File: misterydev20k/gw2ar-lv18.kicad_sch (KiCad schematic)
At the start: 53 parts, among them J3 JTAG, U5 GW2AR-LV18-QN88, U6 W25Q128JVS, U8 SY8113BADC, Y2 27MHz

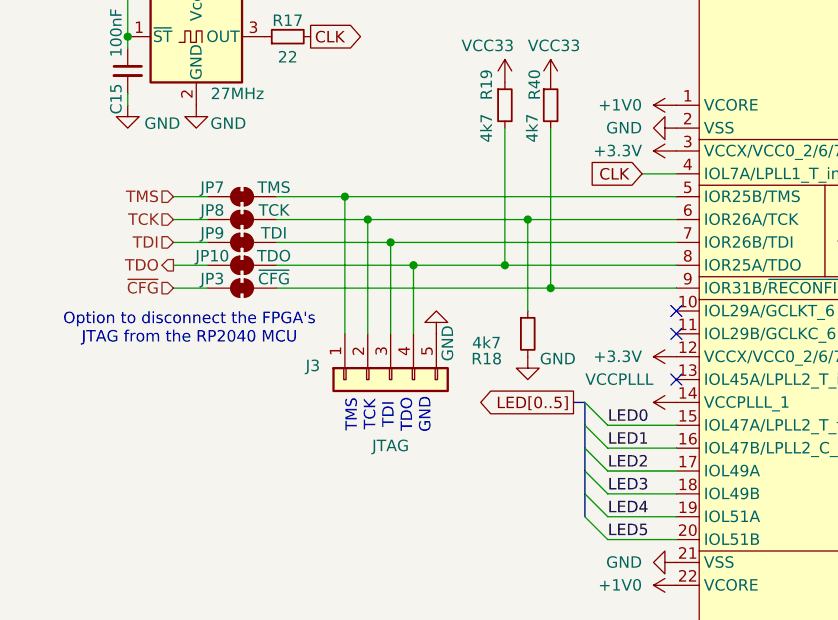
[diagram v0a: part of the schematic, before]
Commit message: Use regular jumpers for JTAG
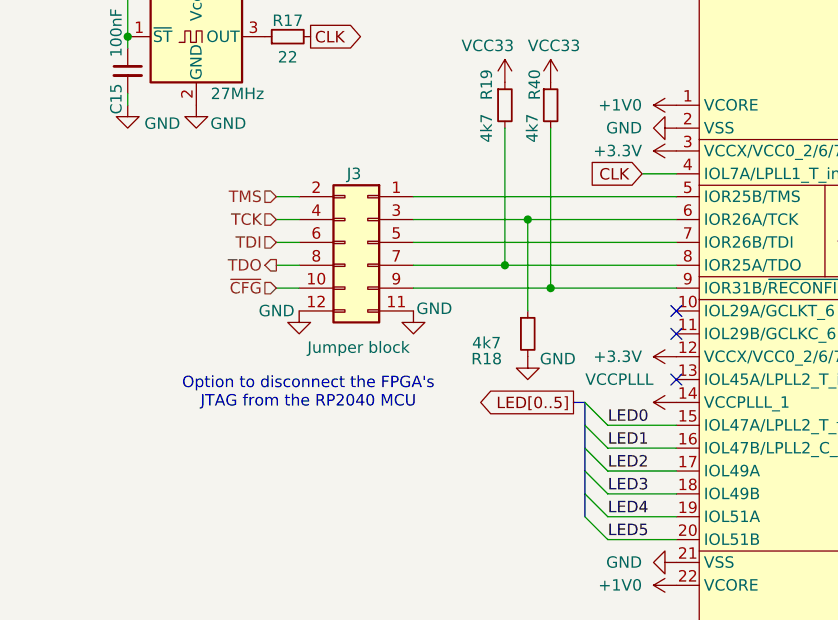
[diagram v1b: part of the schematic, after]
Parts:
- removed J3: JTAG, Connector_PinHeader_2.54mm:PinHeader_1x05_P2.54mm_Vertical, symbol Connector_Generic:Conn_01x05
- removed JP10: TDO, Jumper:SolderJumper-2_P1.3mm_Bridged_RoundedPad1.0x1.5mm, symbol Jumper:SolderJumper_2_Bridged
- removed JP3: ~{CFG}, Jumper:SolderJumper-2_P1.3mm_Bridged_RoundedPad1.0x1.5mm, symbol Jumper:SolderJumper_2_Bridged
- removed JP7: TMS, Jumper:SolderJumper-2_P1.3mm_Bridged_RoundedPad1.0x1.5mm, symbol Jumper:SolderJumper_2_Bridged
- removed JP8: TCK, Jumper:SolderJumper-2_P1.3mm_Bridged_RoundedPad1.0x1.5mm, symbol Jumper:SolderJumper_2_Bridged
- removed JP9: TDI, Jumper:SolderJumper-2_P1.3mm_Bridged_RoundedPad1.0x1.5mm, symbol Jumper:SolderJumper_2_Bridged
- added J3: Jumper block, Connector_PinHeader_2.54mm:PinHeader_2x06_P2.54mm_Vertical, symbol Connector_Generic:Conn_02x06_Odd_Even
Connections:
- net GND: now also J3.11 (Pin_11), J3.12 (Pin_12)
- net TCK: now also J3.4 (Pin_4)
- net TDI: now also J3.6 (Pin_6)
- net TDO: now also J3.8 (Pin_8)
- net TMS: now also J3.2 (Pin_2)
- net ~{CFG}: now also J3.10 (Pin_10)
- net at U5.5 (IOR25B/TMS): now also J3.1 (Pin_1)
- net at R18.1, U5.6 (IOR26A/TCK): now also J3.3 (Pin_3)
- net at U5.7 (IOR26B/TDI): now also J3.5 (Pin_5)
- net at R19.2, U5.8 (IOR25A/TDO): now also J3.7 (Pin_7)
- net at R40.2, U5.9 (IOR31B/~{RECONFIG}): now also J3.9 (Pin_9)
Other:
- note removed: "TMS TCK TDI TDO GND"

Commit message: Update mon tx/rx and spare 5 pins
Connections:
- net VCC33 is gone; now on net +3.3V: R19.1, R40.1
- net JOYB5: now also U5.52 (IOR39A/SCLK); no longer U5.55 (IOR36B/~{SSPI_CS}/D0)
- net SPARE renamed MON_TX
- new net MON_RX: U5.55 (IOR36B/~{SSPI_CS}/D0)
- no-connect marks 11 -> 10
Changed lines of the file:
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@@
 	)
 	(no_connect
-		(at 199.39 97.79)
-	)
-	(no_connect
 		(at 163.83 27.94)
 	)
@@
 	)
 	(bus_entry
-		(at 215.9 90.17)
+		(at 215.9 97.79)
 		(size 2.54 -2.54)
 		(stroke
@@
 	(wire
 		(pts
+			(xy 199.39 90.17) (xy 205.74 90.17)
+		)
+		(stroke
+			(width 0)
+			(type default)
+		)
+	)
+	(wire
+		(pts
 			(xy 118.11 20.32) (xy 118.11 27.94)
 		)
@@
 	(bus
 		(pts
-			(xy 219.71 87.63) (xy 218.44 87.63)
+			(xy 219.71 95.25) (xy 218.44 95.25)
 		)
 		(stroke
@@
 	(wire
 		(pts
-			(xy 199.39 90.17) (xy 215.9 90.17)
+			(xy 199.39 97.79) (xy 215.9 97.79)
 		)
 		(stroke
@@
 	(bus
 		(pts
-			(xy 218.44 87.63) (xy 218.44 102.87)
+			(xy 218.44 95.25) (xy 218.44 102.87)
 		)
 		(stroke
@@
 	)
 	(label "JOYB5"
-		(at 199.39 90.17 0)
+		(at 199.39 97.79 0)
 		(effects
 			(font
@@
 	(global_label "JOYB[0..5]"
 		(shape input)
-		(at 219.71 87.63 0)
+		(at 219.71 95.25 0)
 		(fields_autoplaced yes)
 		(effects
@@
 		)
 		(property "Intersheetrefs" "${INTERSHEET_REFS}"
-			(at 232.0197 87.63 0)
+			(at 232.0197 95.25 0)
 			(effects
 				(font
@@
 		)
 	)
-	(hierarchical_label "SPARE"
-		(shape bidirectional)
+	(hierarchical_label "MON_TX"
+		(shape output)
 		(at 205.74 107.95 0)
 		(effects
@@
 		)
 	)
+	(hierarchical_label "MON_RX"
+		(shape input)
+		(at 205.74 90.17 0)
+		(effects
+			(font
+				(size 1.27 1.27)
+			)
+			(justify left)
+		)
+	)
 	(hierarchical_label "MODE[0..1]"
 		(shape input)
@@
 	)
 	(symbol
-		(lib_name "+3V3_1")
-		(lib_id "power:+3V3")
-		(at 74.93 59.69 0)
-		(unit 1)
-		(exclude_from_sim no)
-		(in_bom yes)
-		(on_board yes)
-		(dnp no)
-		(property "Reference" "#PWR044"
-			(at 74.93 63.5 0)
-			(effects
-				(font
-					(size 1.27 1.27)
-				)
-				(hide yes)
-			)
-		)
-		(property "Value" "VCC33"
-			(at 72.39 55.626 0)
-			(effects
-				(font
-					(size 1.27 1.27)
-				)
-				(justify left)
-			)
-		)
-		(property "Footprint" ""
-			(at 74.93 59.69 0)
-			(effects
-				(font
-					(size 1.27 1.27)
-				)
-				(hide yes)
-			)
-		)
-		(property "Datasheet" ""
-			(at 74.93 59.69 0)
-			(effects
-				(font
-					(size 1.27 1.27)
-				)
-				(hide yes)
-			)
-		)
-		(property "Description" "Power symbol creates a global label with name \"+3V3\""
-			(at 74.93 59.69 0)
-			(effects
-				(font
-					(size 1.27 1.27)
-				)
-				(hide yes)
-			)
-		)
-		(pin "1"
-		)
-		(instances
-			(project "misterydev20k"
-				(path "/ba62e47e-9e07-4e97-ab08-24b670d50f97/1ae93680-6377-49c6-a9eb-78c5d0ac1afd"
-					(reference "#PWR044")
-					(unit 1)
-				)
-			)
-		)
-	)
-	(symbol
 		(lib_id "power:GND")
 		(at 33.02 29.21 90)
@@
 	)
 	(symbol
+		(lib_name "+3V3_1")
+		(lib_id "power:+3V3")
+		(at 74.93 59.69 0)
+		(unit 1)
+		(exclude_from_sim no)
+		(in_bom yes)
+		(on_board yes)
+		(dnp no)
+		(property "Reference" "#PWR054"
+			(at 74.93 63.5 0)
+			(effects
+				(font
+					(size 1.27 1.27)
+				)
+				(hide yes)
+			)
+		)
+		(property "Value" "+3.3V"
+			(at 73.152 55.88 0)
+			(effects
+				(font
+					(size 1.27 1.27)
+				)
+				(justify left)
+			)
+		)
+		(property "Footprint" ""
+			(at 74.93 59.69 0)
+			(effects
+				(font
+					(size 1.27 1.27)
+				)
+				(hide yes)
+			)
+		)
+		(property "Datasheet" ""
+			(at 74.93 59.69 0)
+			(effects
+				(font
+					(size 1.27 1.27)
+				)
+				(hide yes)
+			)
+		)
+		(property "Description" "Power symbol creates a global label with name \"+3V3\""
+			(at 74.93 59.69 0)
+			(effects
+				(font
+					(size 1.27 1.27)
+				)
+				(hide yes)
+			)
+		)
+		(pin "1"
+		)
+		(instances
+			(project "misterydev20k"
+				(path "/ba62e47e-9e07-4e97-ab08-24b670d50f97/1ae93680-6377-49c6-a9eb-78c5d0ac1afd"
+					(reference "#PWR054")
+					(unit 1)
+				)
+			)
+		)
+	)
+	(symbol
 		(lib_id "Jumper:SolderJumper_2_Bridged")
 		(at 237.49 20.32 0)
@@
 	)
 	(symbol
-		(lib_name "+3V3_1")
-		(lib_id "power:+3V3")
-		(at 69.85 59.69 0)
-		(unit 1)
-		(exclude_from_sim no)
-		(in_bom yes)
-		(on_board yes)
-		(dnp no)
-		(property "Reference" "#PWR054"
-			(at 69.85 63.5 0)
-			(effects
-				(font
-					(size 1.27 1.27)
-				)
-				(hide yes)
-			)
-		)
-		(property "Value" "VCC33"
-			(at 65.024 55.626 0)
-			(effects
-				(font
-					(size 1.27 1.27)
-				)
-				(justify left)
-			)
-		)
-		(property "Footprint" ""
-			(at 69.85 59.69 0)
-			(effects
-				(font
-					(size 1.27 1.27)
-				)
-				(hide yes)
-			)
-		)
-		(property "Datasheet" ""
-			(at 69.85 59.69 0)
-			(effects
-				(font
-					(size 1.27 1.27)
-				)
-				(hide yes)
-			)
-		)
-		(property "Description" "Power symbol creates a global label with name \"+3V3\""
-			(at 69.85 59.69 0)
-			(effects
-				(font
-					(size 1.27 1.27)
-				)
-				(hide yes)
-			)
-		)
-		(pin "1"
-		)
-		(instances
-			(project "misterydev20k"
-				(path "/ba62e47e-9e07-4e97-ab08-24b670d50f97/1ae93680-6377-49c6-a9eb-78c5d0ac1afd"
-					(reference "#PWR054")
-					(unit 1)
-				)
-			)
-		)
-	)
-	(symbol
 		(lib_id "power:+3V3")
 		(at 275.59 34.29 0)
@@
 	)
 	(symbol
+		(lib_name "+3V3_1")
+		(lib_id "power:+3V3")
+		(at 69.85 59.69 0)
+		(unit 1)
+		(exclude_from_sim no)
+		(in_bom yes)
+		(on_board yes)
+		(dnp no)
+		(property "Reference" "#PWR044"
+			(at 69.85 63.5 0)
+			(effects
+				(font
+					(size 1.27 1.27)
+				)
+				(hide yes)
+			)
+		)
+		(property "Value" "+3.3V"
+			(at 65.278 55.88 0)
+			(effects
+				(font
+					(size 1.27 1.27)
+				)
+				(justify left)
+			)
+		)
+		(property "Footprint" ""
+			(at 69.85 59.69 0)
+			(effects
+				(font
+					(size 1.27 1.27)
+				)
+				(hide yes)
+			)
+		)
+		(property "Datasheet" ""
+			(at 69.85 59.69 0)
+			(effects
+				(font
+					(size 1.27 1.27)
+				)
+				(hide yes)
+			)
+		)
+		(property "Description" "Power symbol creates a global label with name \"+3V3\""
+			(at 69.85 59.69 0)
+			(effects
+				(font
+					(size 1.27 1.27)
+				)
+				(hide yes)
+			)
+		)
+		(pin "1"
+		)
+		(instances
+			(project "misterydev20k"
+				(path "/ba62e47e-9e07-4e97-ab08-24b670d50f97/1ae93680-6377-49c6-a9eb-78c5d0ac1afd"
+					(reference "#PWR044")
+					(unit 1)
+				)
+			)
+		)
+	)
+	(symbol
 		(lib_id "power:GND")
 		(at 88.9 113.03 270)
@@
 		)
 		(property "Value" "10k"
-			(at 211.328 109.474 90)
+			(at 201.93 111.76 90)
 			(effects
 				(font

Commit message: Update dev20k pinout
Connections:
- net SPARE: now reaches U5.53 (IOR38B/DOUT/~{WE})
- no-connect marks 10 -> 9
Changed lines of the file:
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@@
 	)
 	(no_connect
-		(at 199.39 95.25)
-	)
-	(no_connect
 		(at 88.9 92.71)
 	)
@@
 	(wire
 		(pts
+			(xy 199.39 95.25) (xy 205.74 95.25)
+		)
+		(stroke
+			(width 0)
+			(type default)
+		)
+	)
+	(wire
+		(pts
 			(xy 170.18 154.94) (xy 167.64 154.94)
 		)
@@
 		(effects
 			(font
+				(size 1.27 1.27)
+			)
+			(justify left)
+		)
+	)
+	(hierarchical_label "SPARE"
+		(shape bidirectional)
+		(at 205.74 95.25 0)
+		(effects
+			(font

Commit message: Dev20k LCSC part mapping
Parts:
- added TP1, TP2, TP3, TP4, TP5, TP6, TP7, TP8, TP9: TestPoint, TestPoint:TestPoint_Pad_D1.0mm, symbol Connector:TestPoint
- C15, C16, C17, C27, C35, C36, C4, C42, C44, C46, C47, C48, C49, C50: LCSC C1525 -> (none); LCSC Part # (none) -> C1525; checked (none) -> once
- C33: Comment (none) -> Samsung 10V X5R; LCSC C52923 -> (none); LCSC Part # (none) -> C19702; checked (none) -> once
- C34, C39: LCSC C1525 -> (none); LCSC Part # (none) -> C14663; checked (none) -> once
- C37: LCSC C1525 -> (none); LCSC Part # (none) -> C1555; checked (none) -> once
- C38: Comment (none) -> Murata 10V X5R; LCSC C52923 -> (none); LCSC Part # (none) -> C84419; checked (none) -> once
- C41, C43: value 4u7 -> 10uF; Comment (none) -> Samsung 6.3V X5R; LCSC Part # (none) -> C15525; checked (none) -> once
- FB3, FB4: LCSC C107332 -> (none); LCSC Part # (none) -> C107332; checked (none) -> once
- J3: LCSC Part # (none) -> C6837606; checked (none) -> once
- L1: LCSC C408336 -> (none); LCSC Part # (none) -> C408336; checked (none) -> once
- R17, R26, R52: LCSC C11702 -> (none); LCSC Part # (none) -> C25092; checked (none) -> once
- R18, R19, R29, R31, R32, R40: LCSC C11702 -> (none); LCSC Part # (none) -> C25900; checked (none) -> once
- R22: LCSC C11702 -> (none); LCSC Part # (none) -> C25744; checked (none) -> once
- R30, R37: LCSC C11702 -> (none); LCSC Part # (none) -> C11702; checked (none) -> once
- R38: LCSC C11702 -> (none); LCSC Part # (none) -> C138008; checked (none) -> once
- R39: LCSC Part # (none) -> C25752; checked (none) -> once
- R56: LCSC Part # (none) -> C138044; checked (none) -> once
- U6: LCSC C131025 -> (none); LCSC Part # (none) -> C131025; checked (none) -> once
- U8: LCSC Part # (none) -> C78989; checked (none) -> once
- Y2: checked (none) -> once
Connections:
- net at U5.10 (IOL29A/GCLKT_6): now also TP7.1
- net at U5.11 (IOL29B/GCLKC_6): now also TP8.1
- net at U5.13 (IOL45A/LPLL2_T_in): now also TP9.1
- net at U5.32 (IOB18B): now also TP1.1
- net at U5.69 (IOT50A): now also TP6.1
- net at U5.70 (IOT44B): now also TP5.1
- net at U5.75 (IOT34A): now also TP4.1
- net at U5.76 (IOT30B/GCLKC_1): now also TP3.1
- net at U5.86 (IOT4A): now also TP2.1
- no-connect marks 9 -> 0

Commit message: Update debug UART wiring
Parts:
- removed TP5: TestPoint, TestPoint:TestPoint_Pad_D1.0mm, symbol Connector:TestPoint
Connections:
- net UART_RX: now also U5.70 (IOT44B); no longer U5.72 (IOT40B)
- net UART_TX: now also J3.7 (Pin_7), R19.2, U5.8 (IOR25A/TDO); no longer U5.71 (IOT44A)
- new net MIDI_IN: U5.72 (IOT40B)
- new net MIDI_OUT: U5.71 (IOT44A)
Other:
- sheet Interfaces ports: added MIDI_IN, MIDI_OUT, MON_RX, MON_TX; removed UART_RX, UART_TX
- moved on the sheet: C27, R29, R30, R31, R32, U6

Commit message: Fix JLCPCB footprint offset and rotation
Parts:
- J3: FT Rotation Offset (none) -> 90; LCSC Part # C6837606 -> C32713279
- U5: LCSC Part # (none) -> C9900028472; checked (none) -> once
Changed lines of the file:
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@@
 			)
 		)
-		(property "checked" ""
+		(property "checked" "once"
+			(at 144.78 88.9 0)
+			(effects
+				(font
+					(size 1.27 1.27)
+				)
+				(hide yes)
+			)
+		)
+		(property "LCSC Part #" "C9900028472"
 			(at 144.78 88.9 0)
 			(effects
@@
 			)
 		)
-		(property "LCSC Part #" "C6837606"
+		(property "LCSC Part #" "C32713279"
 			(at 54.61 77.47 0)
 			(effects
+				(font
+					(size 1.27 1.27)
+				)
+				(hide yes)
+			)
+		)
+		(property "FT Rotation Offset" "90"
+			(at 54.61 77.47 0)
+			(effects

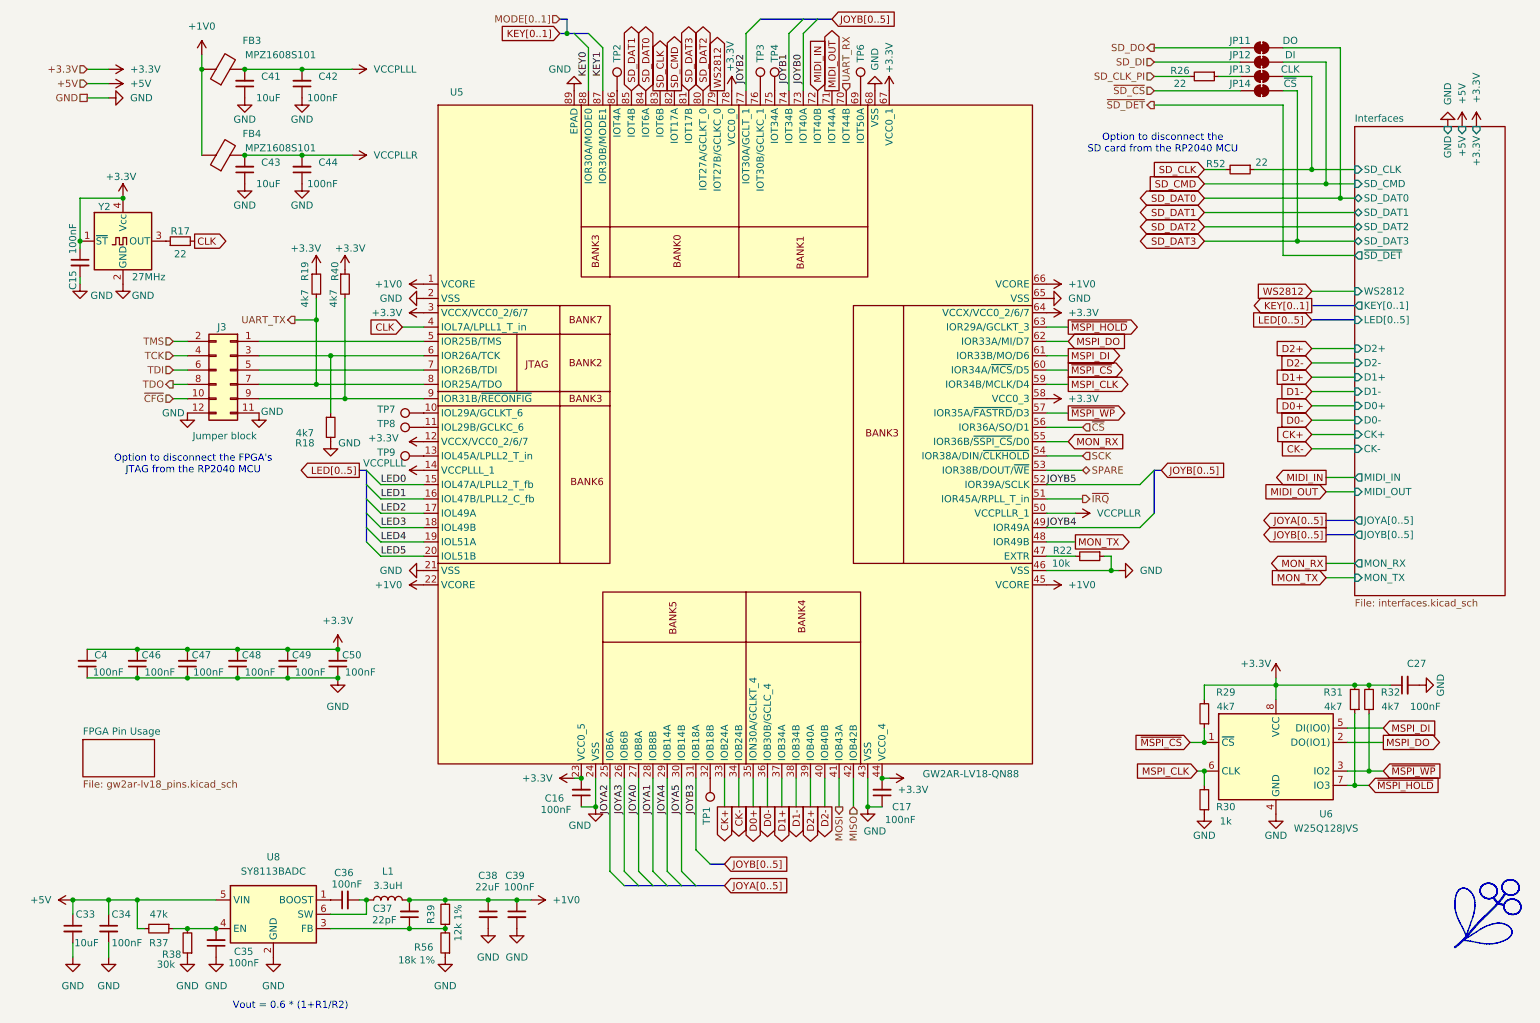
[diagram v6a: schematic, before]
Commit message: Add hyperram
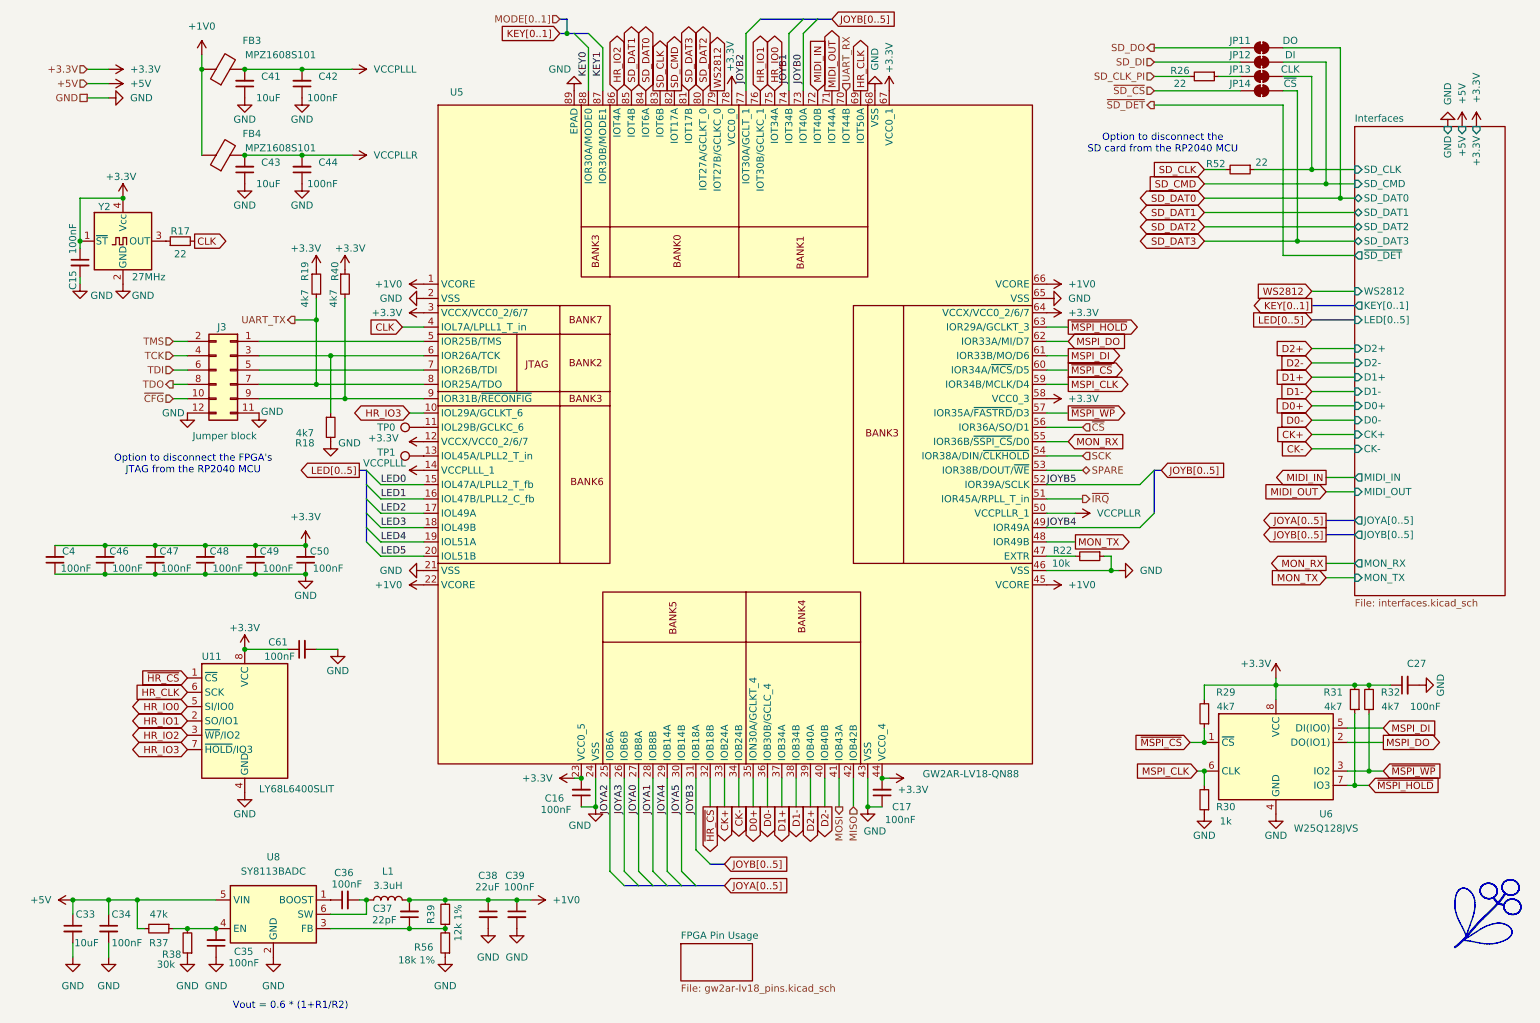
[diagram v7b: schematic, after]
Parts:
- removed TP1, TP2, TP3, TP4, TP6, TP7: TestPoint, TestPoint:TestPoint_Pad_D1.0mm, symbol Connector:TestPoint
- added C61: 100nF, Capacitor_SMD:C_0402_1005Metric, symbol Device:C_Small
- added U11: LY68L6400SLIT, Package_SO:SOIC-8_3.9x4.9mm_P1.27mm, symbol Memory_Flash:AT25SF081-SSHD-X
- renumbered TP8 to TP0, TP9 to TP1
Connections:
- net +3.3V: now also C61.1, U11.8 (VCC)
- net GND: now also C61.2, U11.4 (GND)
- net HR_IO3: now reaches U5.10 (IOL29A/GCLKT_6)
- net HR_IO3: now also U11.7 (~{HOLD}/IO3)
- net ~{HR_CS}: now reaches U5.32 (IOB18B)
- net ~{HR_CS}: now also U11.1 (~{CS})
- net HR_CLK: now reaches U5.69 (IOT50A)
- net HR_CLK: now also U11.6 (SCK)
- net HR_IO0: now reaches U5.75 (IOT34A)
- net HR_IO0: now also U11.5 (SI/IO0)
- net HR_IO1: now reaches U5.76 (IOT30B/GCLKC_1)
- net HR_IO1: now also U11.2 (SO/IO1)
- net HR_IO2: now reaches U5.86 (IOT4A)
- net HR_IO2: now also U11.3 (~{WP}/IO2)
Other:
- moved on the sheet: C4, C46, C47, C48, C49, C50
